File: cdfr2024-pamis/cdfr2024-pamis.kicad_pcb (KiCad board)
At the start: 4 copper layers, 24 parts, among them J1 Connecteur batterie, J2 Conn_ST_STDC14, J3 Connecteur Programmation, J4 Connecteur Débug, J5 Connecteur ToF, J6 Moteur Droit, J7 Moteur Gauche, U1 STM32F401RCTx, U2 LM317_SOT-223, U4 Driver Moteur Droit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

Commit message: Refonte dossier
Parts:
- moved J7 67.4 mm to (76.2, 48.3)
- moved J6 67.3 mm to (121.9, 48.3)
- moved J5 61.7 mm to (78.7, 35.6), turned to 90 degrees
- moved U1 52.9 mm to (89.5, 48.9), turned to 180 degrees
- moved J3 51.6 mm to (121.9, 68.6)
- moved U4 49.0 mm to (111.8, 50.8)
- moved U2 46.6 mm to (61.0, 71.7), turned to -90 degrees
- moved U5 41.7 mm to (66.0, 50.8)
- moved R1 36.0 mm to (99.1, 74.7), turned to 90 degrees
- moved D1 34.9 mm to (87.4, 76.2)
- moved C7 31.9 mm to (70.1, 78.7)
- moved C8 31.9 mm to (70.1, 81.8)
- moved C6 28.9 mm to (74.7, 78.7), turned to 180 degrees
- moved R4 28.5 mm to (109.2, 90.4), turned to 90 degrees
- moved C5 28.5 mm to (70.1, 76.2)
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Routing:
- net +3.3V: track 0.00 -> 294.9 mm, vias 0 -> 3
- net GND: track 0.00 -> 258.5 mm, vias 0 -> 7
- net +7.5V: track 0.00 -> 171.3 mm
- net SWDIO: track 0.00 -> 86.8 mm, vias 0 -> 1
- net /RX: track 0.00 -> 73.8 mm, vias 0 -> 2
- net Net-(U2-ADJ): track 0.00 -> 73.6 mm
- net /TX: track 0.00 -> 61.5 mm, vias 0 -> 2
- net RST: track 0.00 -> 56.9 mm, vias 0 -> 2
- net Net-(U1-PA7): track 0.00 -> 56.0 mm, vias 0 -> 1
- net Net-(U1-PA5): track 0.00 -> 54.7 mm, vias 0 -> 1
- net SWCLK: track 0.00 -> 47.5 mm
- net Net-(U1-BOOT0): track 0.00 -> 45.8 mm, vias 0 -> 2
- net Net-(U1-PA8): track 0.00 -> 44.3 mm
- net Net-(U1-PA9): track 0.00 -> 42.5 mm
- net Net-(U1-PA10): track 0.00 -> 41.9 mm
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
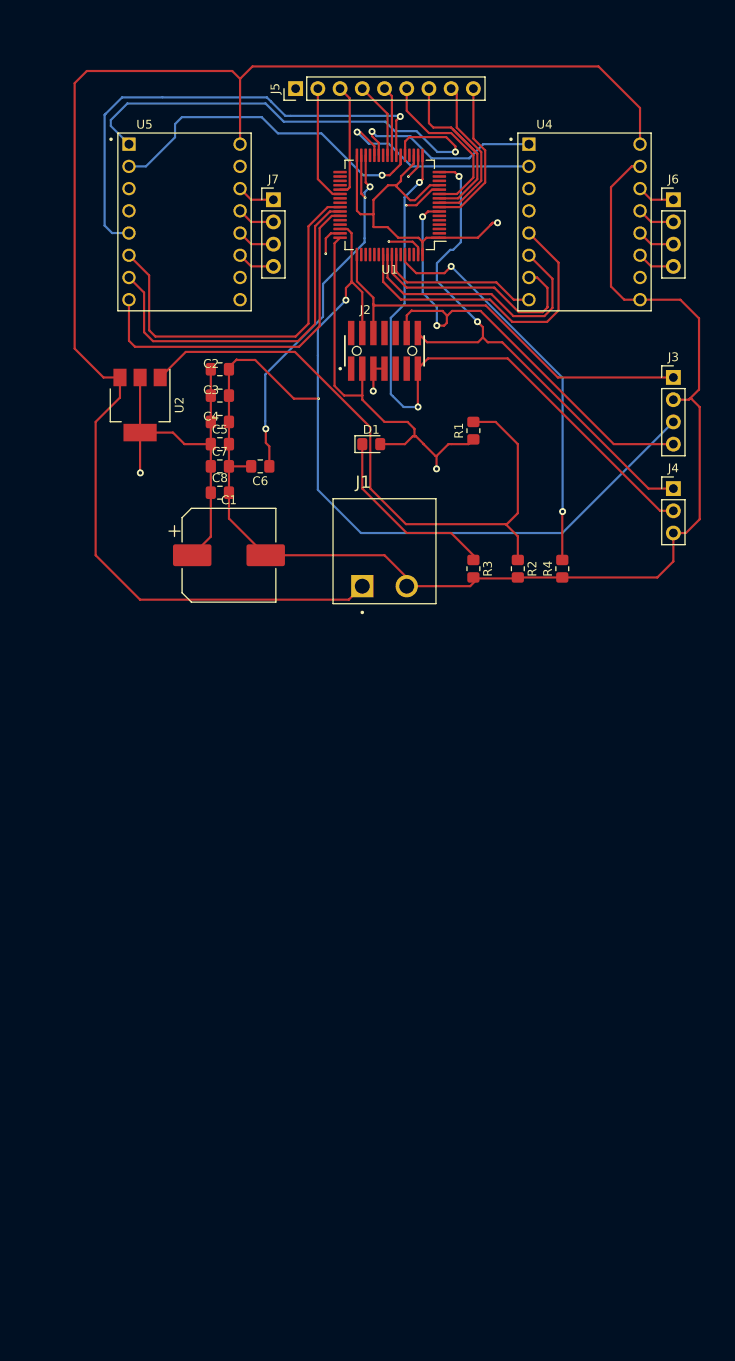
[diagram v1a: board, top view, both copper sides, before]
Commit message: - supression des messages d'erreur dans le schema - Suppression es message d'erreur sur PCB - modification des regles - modification du contour
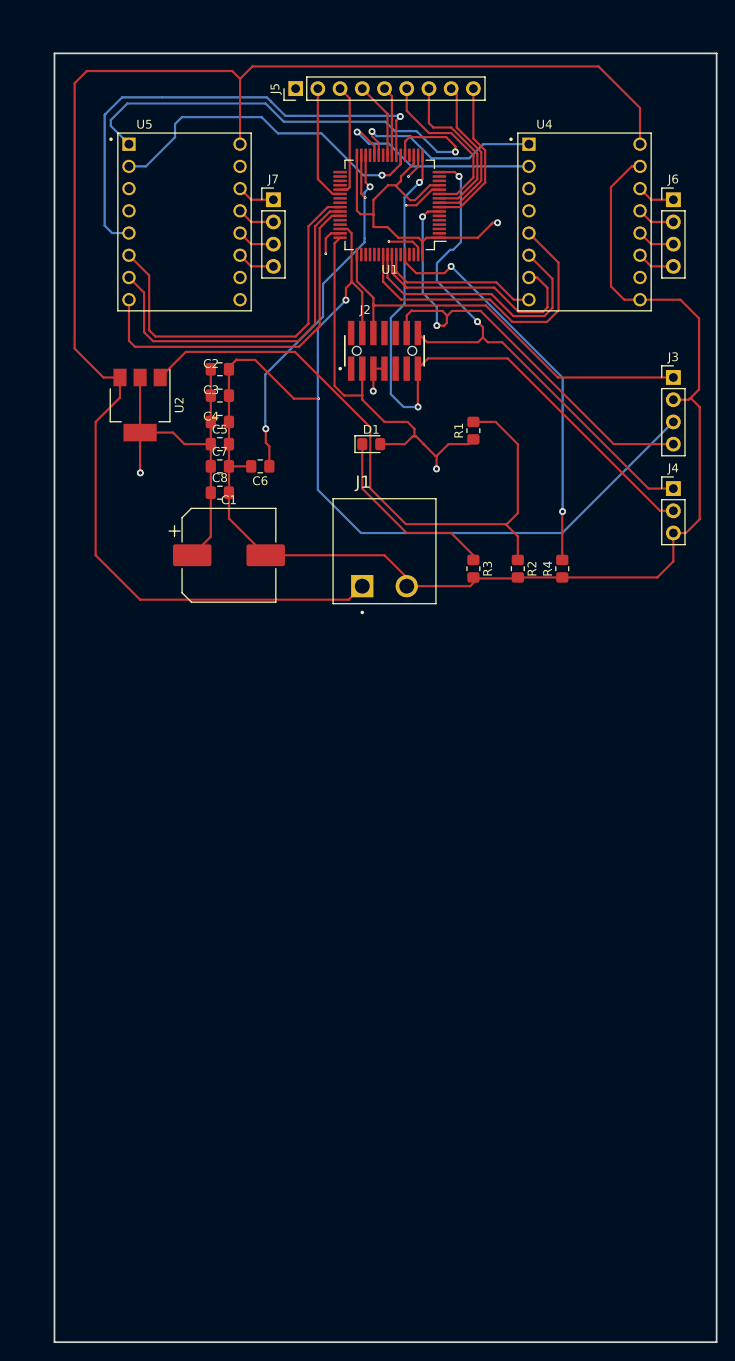
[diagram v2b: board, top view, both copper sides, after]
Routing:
- net Net-(J5-Pin_7): track 22.9 -> 19.1 mm
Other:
- board outline added: 75.7 x 147.3 mm
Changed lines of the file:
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@@
   )
   (gr_rect (start 51.173 31.535) (end 126.865 178.855)
-    (stroke (width 0.2) (type default)) (fill none) (layer "In1.Cu"))
+    (stroke (width 0.2) (type default)) (fill none) (layer "Edge.Cuts"))
   (segment (start 94.849909 77.556616) (end 94.728991 77.556616) (width 0.25) (layer "F.Cu") (net 1))
   (segment (start 69.045 70.65) (end 69.045 73.66) (width 0.25) (layer "F.Cu") (net 1))
@@
   (segment (start 83.188667 53.236333) (end 83.188667 69.550445) (width 0.25) (layer "F.Cu") (net 1))
   (segment (start 89.247627 51.390291) (end 90.464308 52.606972) (width 0.25) (layer "F.Cu") (net 1))
-  (segment (start 91.231255 76.2) (end 91.246762 76.2) (width 0.25) (layer "F.Cu") (net 1))
   (segment (start 83.82 52.605) (end 83.188667 53.236333) (width 0.25) (layer "F.Cu") (net 1))
   (segment (start 60.990371 79.488245) (end 60.96 79.457874) (width 0.25) (layer "F.Cu") (net 1))
@@
   (segment (start 97.311396 48.105) (end 95.17 48.105) (width 0.25) (layer "F.Cu") (net 22))
   (segment (start 99.378198 42.861802) (end 99.51 42.993604) (width 0.25) (layer "F.Cu") (net 22))
-  (segment (start 96.706396 40.19) (end 99.378198 42.861802) (width 0.25) (layer "F.Cu") (net 22))
   (segment (start 99.51 45.906396) (end 97.311396 48.105) (width 0.25) (layer "F.Cu") (net 22))
   (segment (start 93.98 35.56) (end 93.98 39.511406) (width 0.25) (layer "F.Cu") (net 22))

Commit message: "Rapprochement capas 100nF + plan de masse + tous de fixation"
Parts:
- moved C5 42.3 mm to (95.5, 42.4)
- moved C3 31.1 mm to (96.7, 54.6), turned to 180 degrees
- moved C2 26.9 mm to (81.3, 43.2), turned to 180 degrees
- moved C4 22.8 mm to (81.8, 54.1), turned to 90 degrees
- moved C7 2.29 mm to (70.1, 76.5)
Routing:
- net GND: track 258.5 -> 274.6 mm
- net +7.5V: track 171.3 -> 156.1 mm
- net Net-(U1-PA5): track 54.7 -> 41.9 mm
- net +3.3V: track 294.9 -> 301.6 mm, vias 3 -> 5
- net Net-(U1-PA9): track 42.5 -> 40.7 mm
- net Net-(U1-PA8): track 44.3 -> 42.5 mm
- net Net-(U1-PA10): track 41.9 -> 40.2 mm
- net SWDIO: track 86.8 -> 87.8 mm
- added copper zone on In1.Cu, net GND
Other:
- board size 75.7 x 147.3 mm -> 75.7 x 64.3 mm

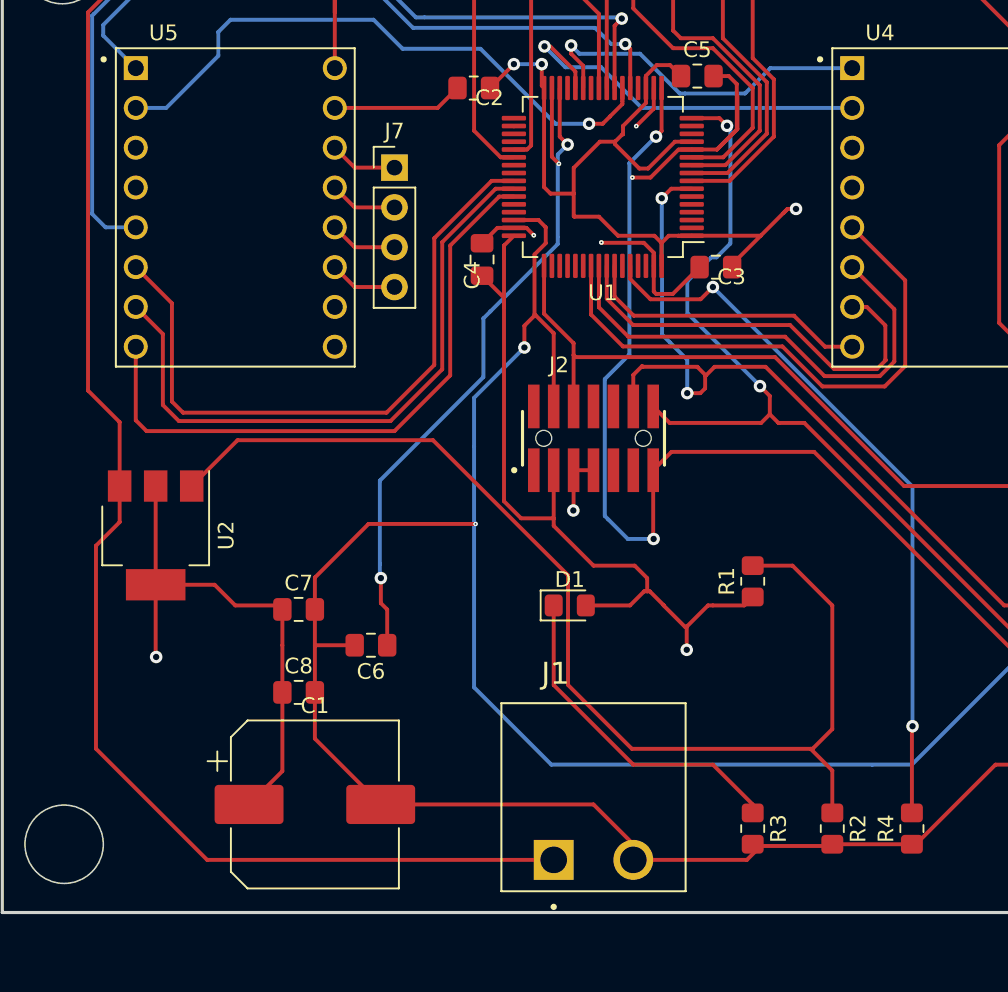
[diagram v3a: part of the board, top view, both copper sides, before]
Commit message: changement de sens connecteur alim IN
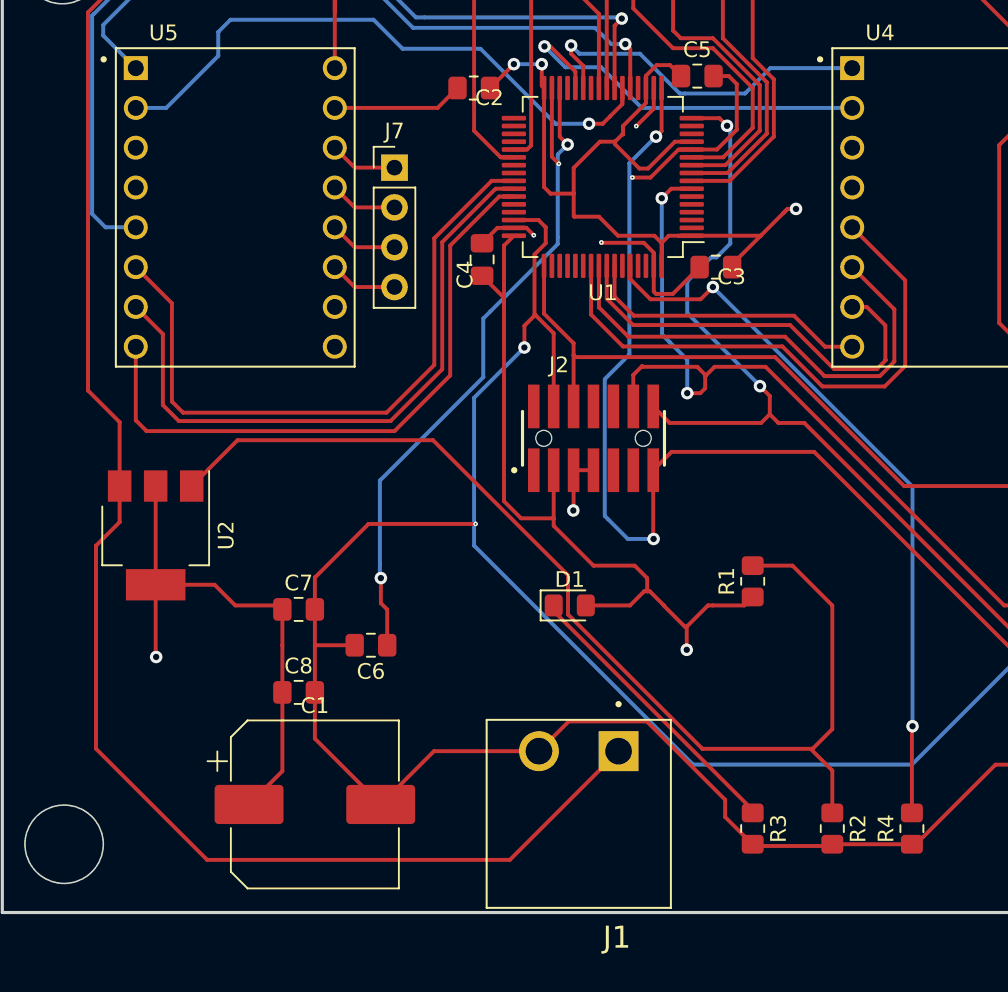
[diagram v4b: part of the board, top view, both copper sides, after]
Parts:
- moved J1 8.08 mm to (90.5, 85.5), turned to 180 degrees
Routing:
- net +7.5V: track 156.1 -> 162.9 mm
- net SWDIO: track 87.8 -> 82.5 mm
- net Net-(D1-K): track 21.5 -> 18.5 mm
- net Net-(U2-ADJ): track 73.6 -> 70.9 mm
- net GND: track 274.6 -> 273.8 mm
- net +3.3V: track 301.6 -> 300.8 mm

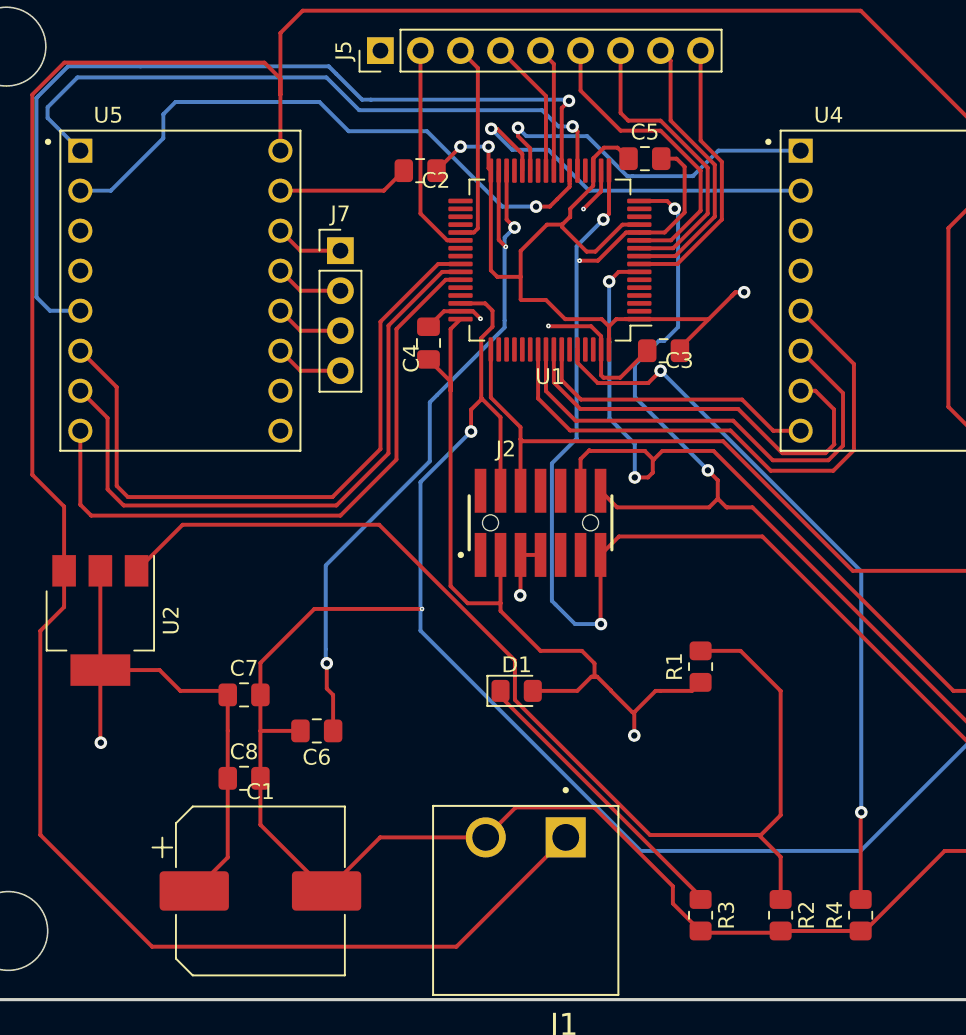
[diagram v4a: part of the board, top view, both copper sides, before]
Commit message: Change via sizes, only through vias
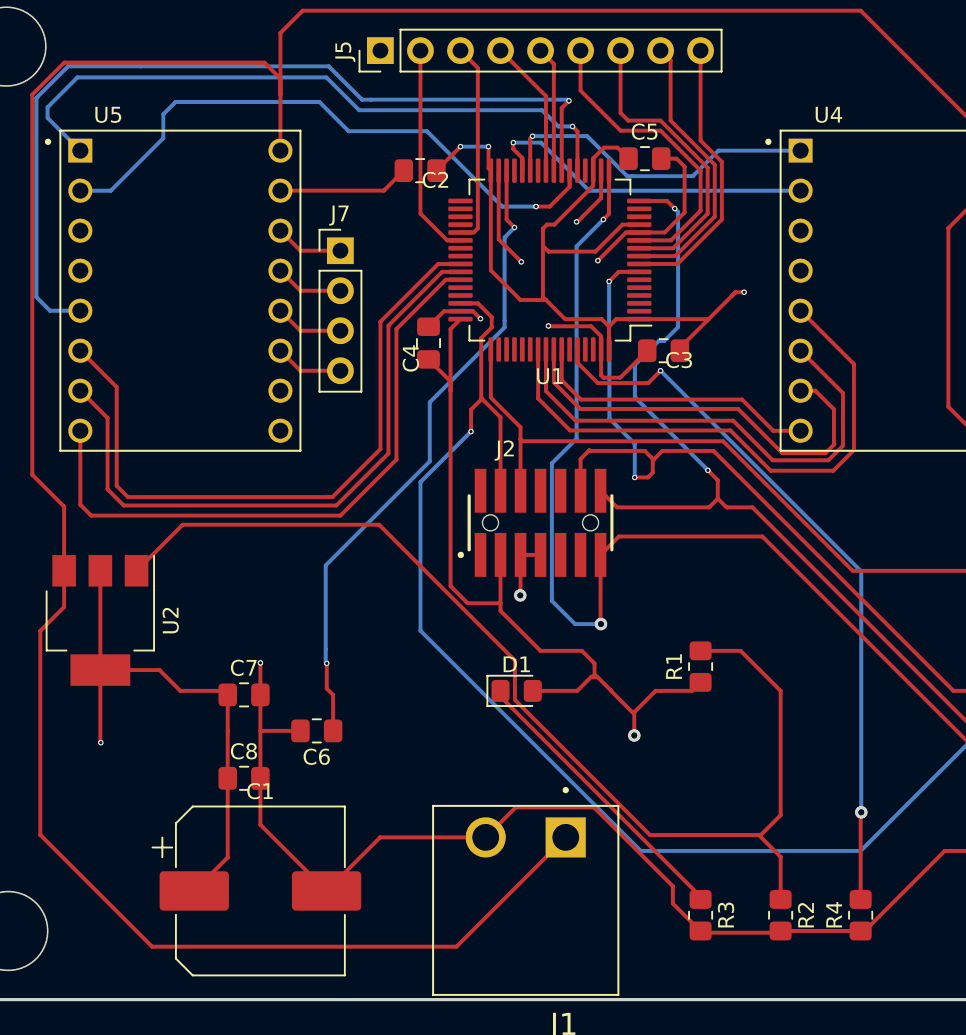
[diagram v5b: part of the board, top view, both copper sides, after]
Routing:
- net GND: track 273.8 -> 224.5 mm
- net Net-(U1-PB2): track 25.0 -> 21.5 mm
- net Net-(U1-PB1): track 22.9 -> 21.0 mm

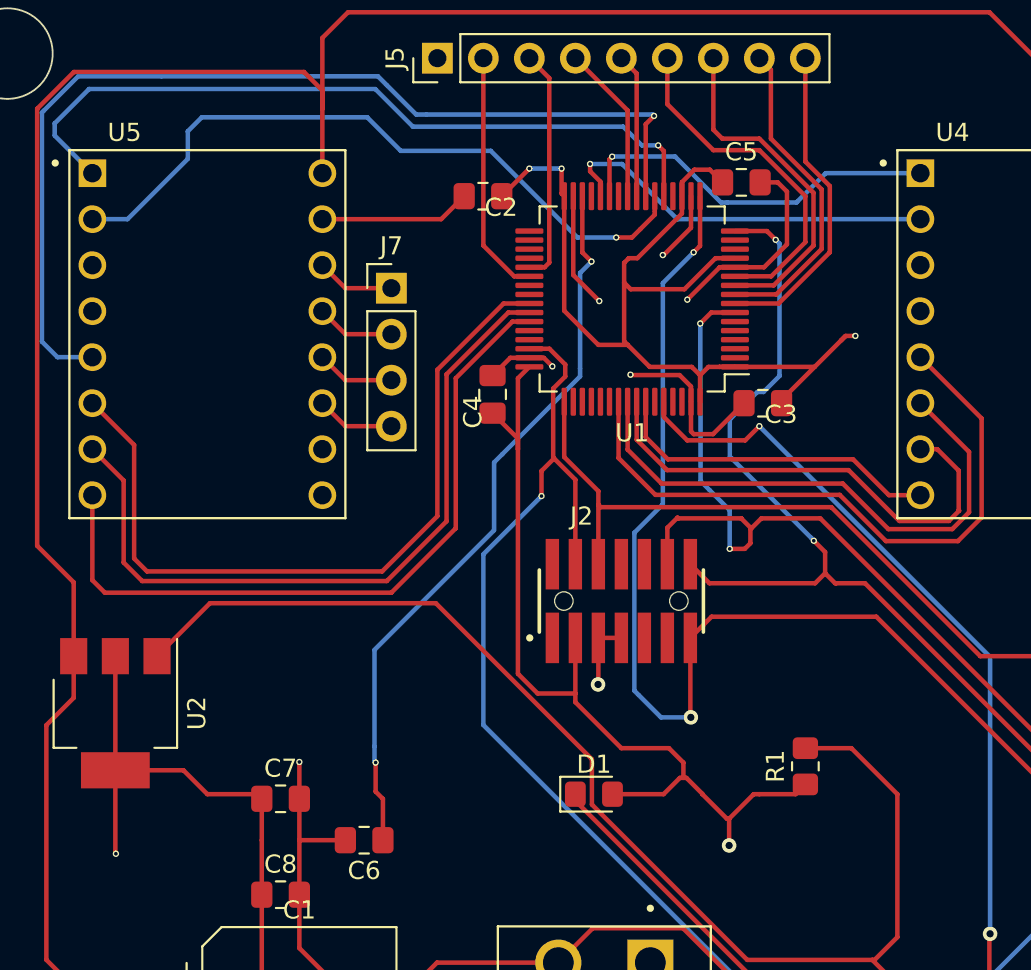
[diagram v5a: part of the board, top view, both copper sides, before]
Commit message: Resize vias again
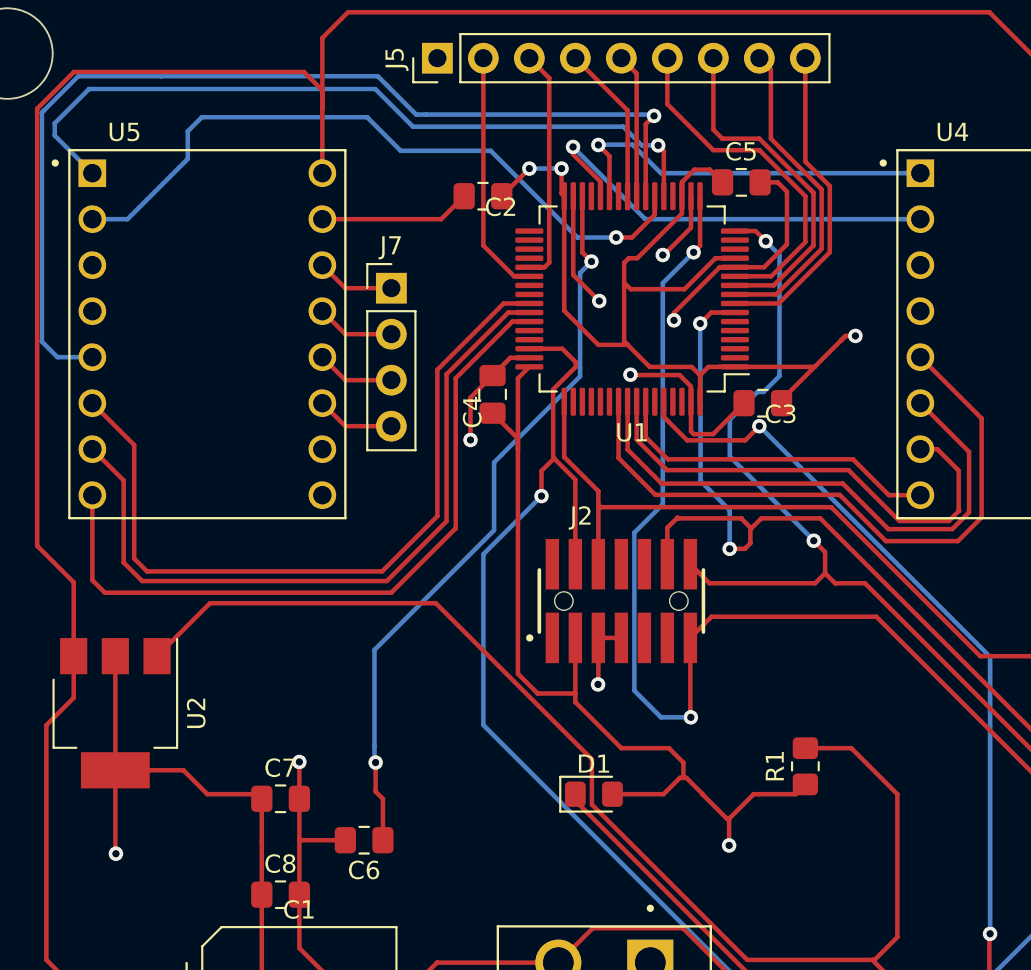
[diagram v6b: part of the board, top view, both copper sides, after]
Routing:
- net Net-(U1-PB2): track 21.5 -> 24.2 mm
- net GND: track 224.5 -> 223.4 mm
- net SWDIO: track 82.2 -> 83.1 mm
- net Net-(U1-PB1): track 21.0 -> 21.5 mm
